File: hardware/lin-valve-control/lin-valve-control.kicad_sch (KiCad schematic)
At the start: 25 parts, among them J1 UPDI, J2 I2C LCD, J3 Screw_Terminal_01x03, Q1 2N7002, Q2 2N7002, U1 TJA1021T, U2 ATtiny824-X, U3 PCA9536DP

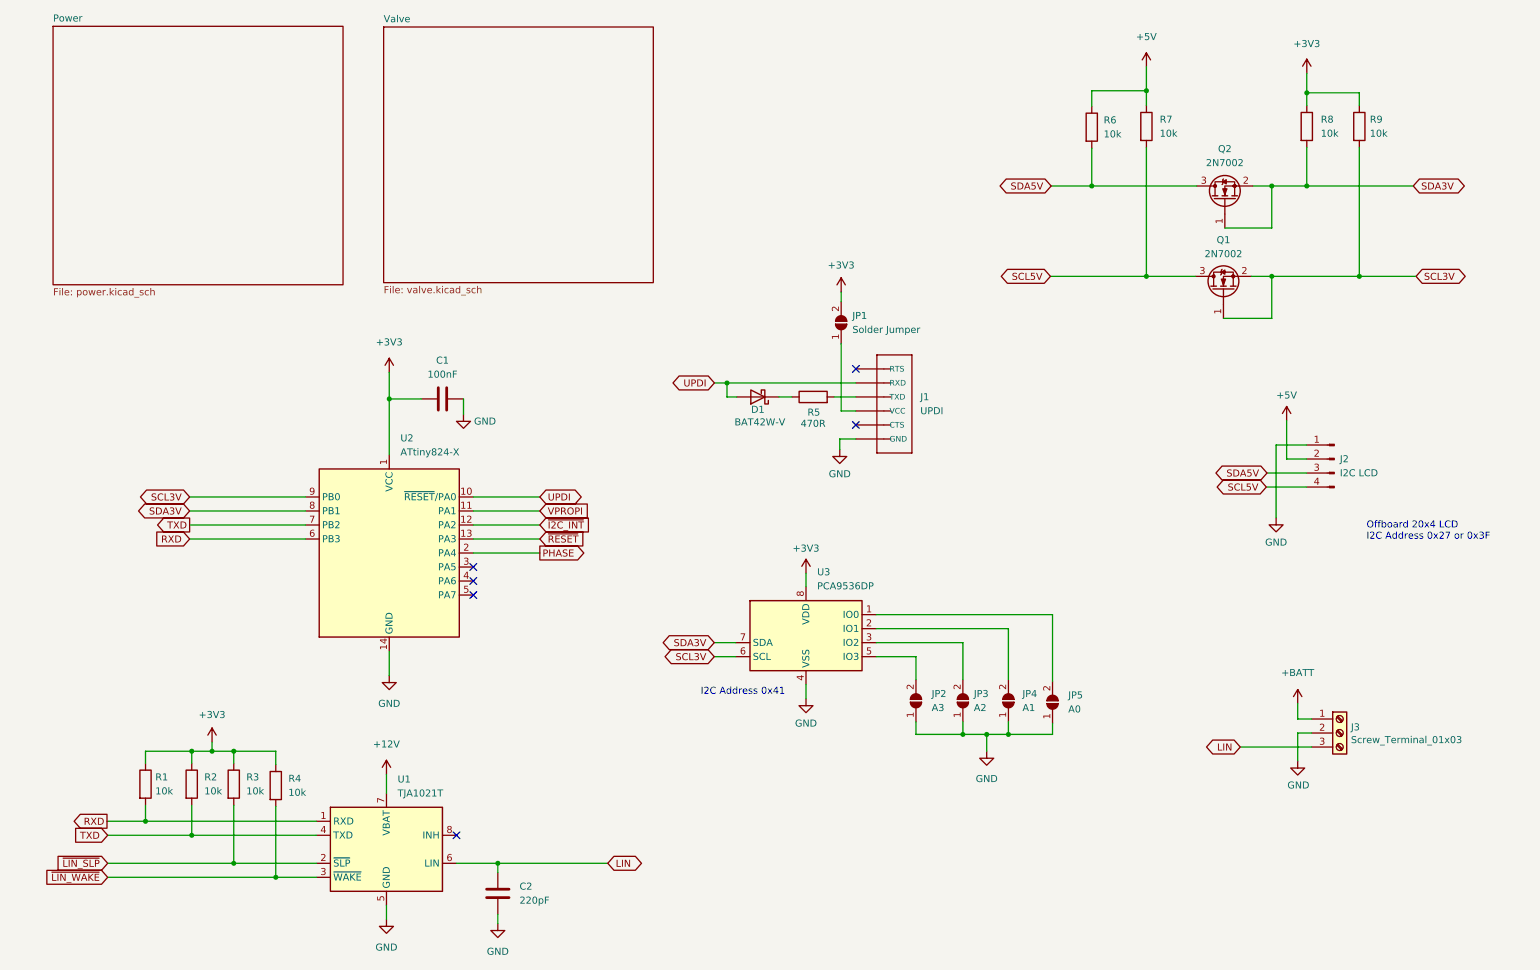
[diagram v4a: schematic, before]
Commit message: Rework valve-controller board, simplify firmware
- linbus_interface and linbus_registers moved to the common lib.
- reworked them all to compile again
- removing PCA9536 from all boards, adding the voltage reg. module
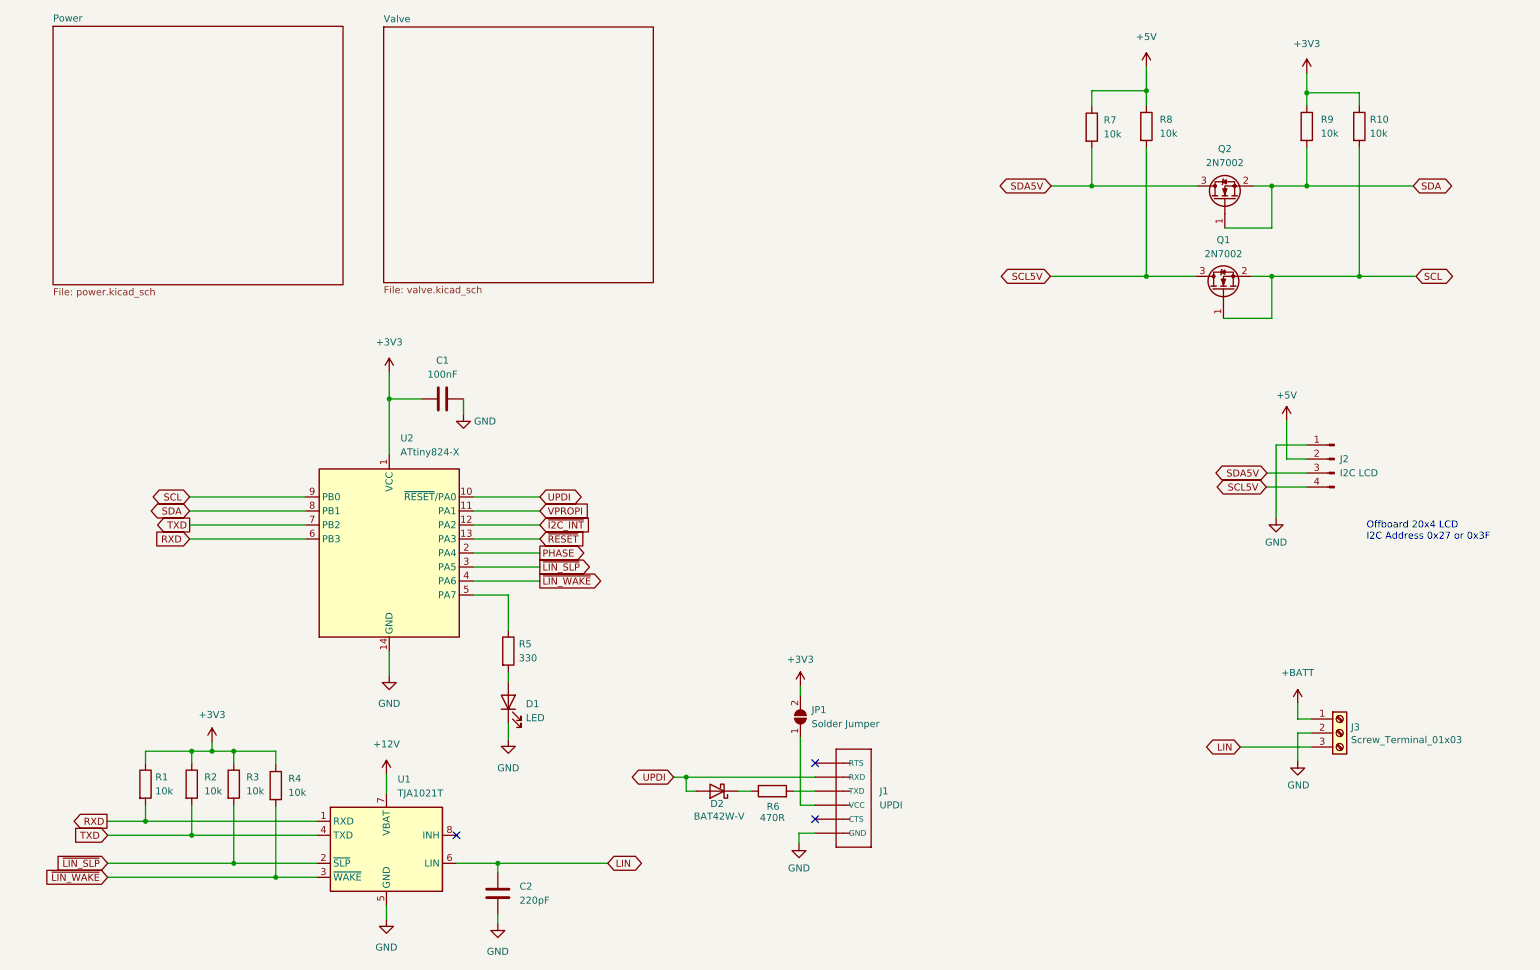
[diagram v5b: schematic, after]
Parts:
- removed JP2: A3, Jumper:SolderJumper-2_P1.3mm_Open_TrianglePad1.0x1.5mm, symbol Jumper:SolderJumper_2_Open
- removed JP3: A2, Jumper:SolderJumper-2_P1.3mm_Open_TrianglePad1.0x1.5mm, symbol Jumper:SolderJumper_2_Open
- removed JP4: A1, Jumper:SolderJumper-2_P1.3mm_Open_TrianglePad1.0x1.5mm, symbol Jumper:SolderJumper_2_Open
- removed JP5: A0, Jumper:SolderJumper-2_P1.3mm_Open_TrianglePad1.0x1.5mm, symbol Jumper:SolderJumper_2_Open
- removed U3: PCA9536DP, Package_SO:TSSOP-8_3x3mm_P0.65mm, symbol Interface_Expansion:PCA9536DP
- added D1: LED, LED_SMD:LED_0805_2012Metric_Pad1.15x1.40mm_HandSolder, symbol Device:LED
- added R5: 330, Resistor_SMD:R_0805_2012Metric_Pad1.20x1.40mm_HandSolder, symbol Device:R
- J1: footprint Beirdo:FTDI_BASIC -> Beirdo:FTDI-TARGET
- renumbered D1 to D2, R9 to R10, R5 to R6, R6 to R7, R7 to R8, R8 to R9
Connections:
- net GND: now also D1.1 (K)
- net ~{LIN_SLP}: now also U2.3 (PA5)
- net ~{LIN_WAKE}: now also U2.4 (PA6)
- net at U2.5 (PA7): now also R5.1
- net SCL3V renamed SCL
- net SDA3V renamed SDA
- new net: D1.2 (A), R5.2
- no-connect marks 6 -> 3
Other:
- note removed: "I2C Address 0x41"
- moved on the sheet: D2, J1, JP1, R6

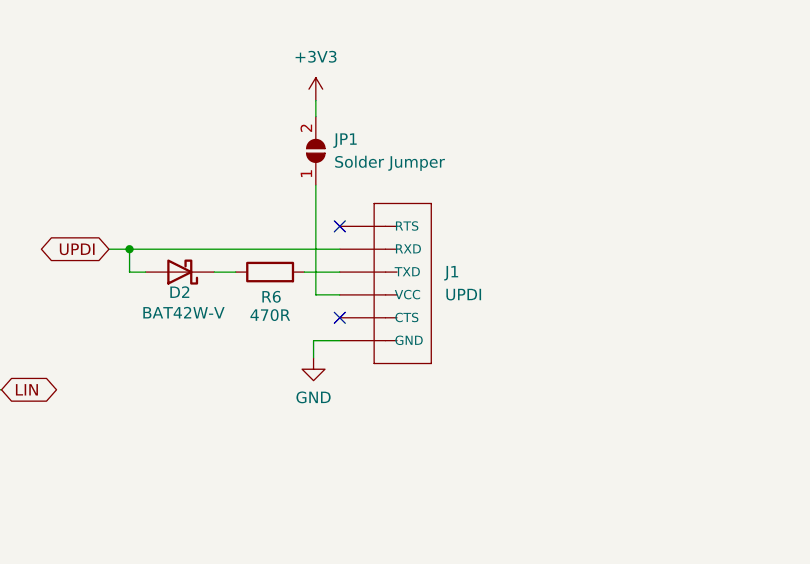
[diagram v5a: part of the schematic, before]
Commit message: Update the schematics... remove PCA9536, use voltage regulator
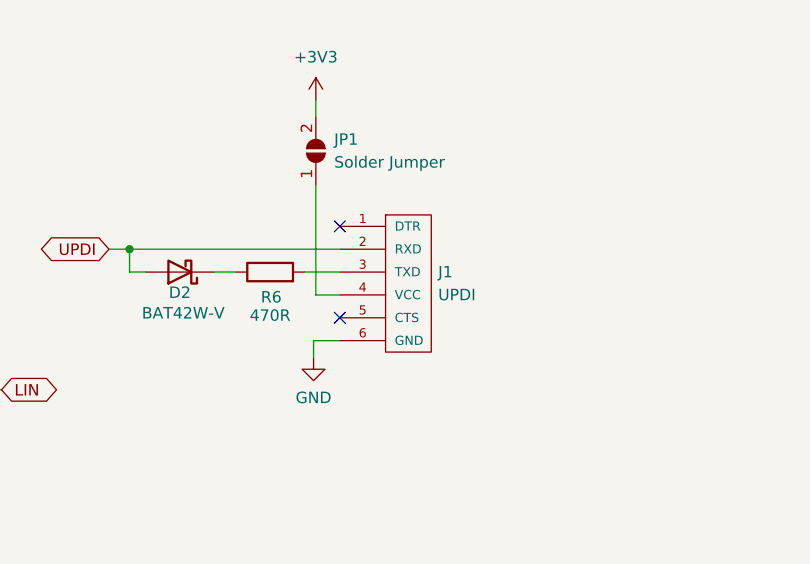
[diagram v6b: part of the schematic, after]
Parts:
- J1: symbol Beirdo:FTDI_BASICPTH -> Beirdo:FTDI-TARGET
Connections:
- net GND: now also J1.6 (GND); no longer J1.1 (GND)
- net UPDI: now also J1.2 (RXD); no longer J1.5 (RXD)
- net at J1.3 (TXD): now also R6.2; no longer JP1.1 (A)
- net at J1.4 (VCC): now also JP1.1 (A); no longer R6.2
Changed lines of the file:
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@@
-    (stroke (width 0) (type default) (color 0 0 0 0))
-  )
-  (wire (pts (xy 156.718 165.989) (xy 153.797 165.989))
     (stroke (width 0) (type default) (color 0 0 0 0))
   )
@@
     (stroke (width 0) (type default) (color 0 0 0 0))
   )
+  (wire (pts (xy 153.797 165.989) (xy 156.718 165.989))
+    (stroke (width 0) (type default) (color 0 0 0 0))
+  )
   (wire (pts (xy 79.502 82.423) (xy 79.502 87.249))
     (stroke (width 0) (type default) (color 0 0 0 0))
@@
     (stroke (width 0) (type default) (color 0 0 0 0))
   )
-  (wire (pts (xy 156.718 160.909) (xy 154.051 160.909))
+  (wire (pts (xy 154.051 160.909) (xy 156.718 160.909))
     (stroke (width 0) (type default) (color 0 0 0 0))
   )
@@
     (pin "2")
   )
-  (symbol (lib_id "Beirdo:FTDI_BASICPTH") (at 161.798 160.909 0) (mirror y) (unit 1)
+  (symbol (lib_id "Beirdo:FTDI-TARGET") (at 164.338 152.019 0) (unit 1)
     (in_bom yes) (on_board yes) (fields_autoplaced)
-    (property "Reference" "J1" (id 0) (at 168.402 158.3689 0)
-      (effects (font (size 1.27 1.27)) (justify right))
-    )
-    (property "Value" "UPDI" (id 1) (at 168.402 160.9089 0)
-      (effects (font (size 1.27 1.27)) (justify right))
-    )
-    (property "Footprint" "Beirdo:FTDI-TARGET" (id 2) (at 161.036 157.099 0)
+    (property "Reference" "J1" (id 0) (at 167.64 158.3689 0)
+      (effects (font (size 1.27 1.27)) (justify left))
+    )
+    (property "Value" "UPDI" (id 1) (at 167.64 160.9089 0)
+      (effects (font (size 1.27 1.27)) (justify left))
+    )
+    (property "Footprint" "Beirdo:FTDI-TARGET" (id 2) (at 164.338 171.069 0)
       (effects (font (size 0.508 0.508)) hide)
     )
